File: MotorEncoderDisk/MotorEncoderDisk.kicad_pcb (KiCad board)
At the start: 2 copper layers, 28.2 x 28.2 mm, 1 part

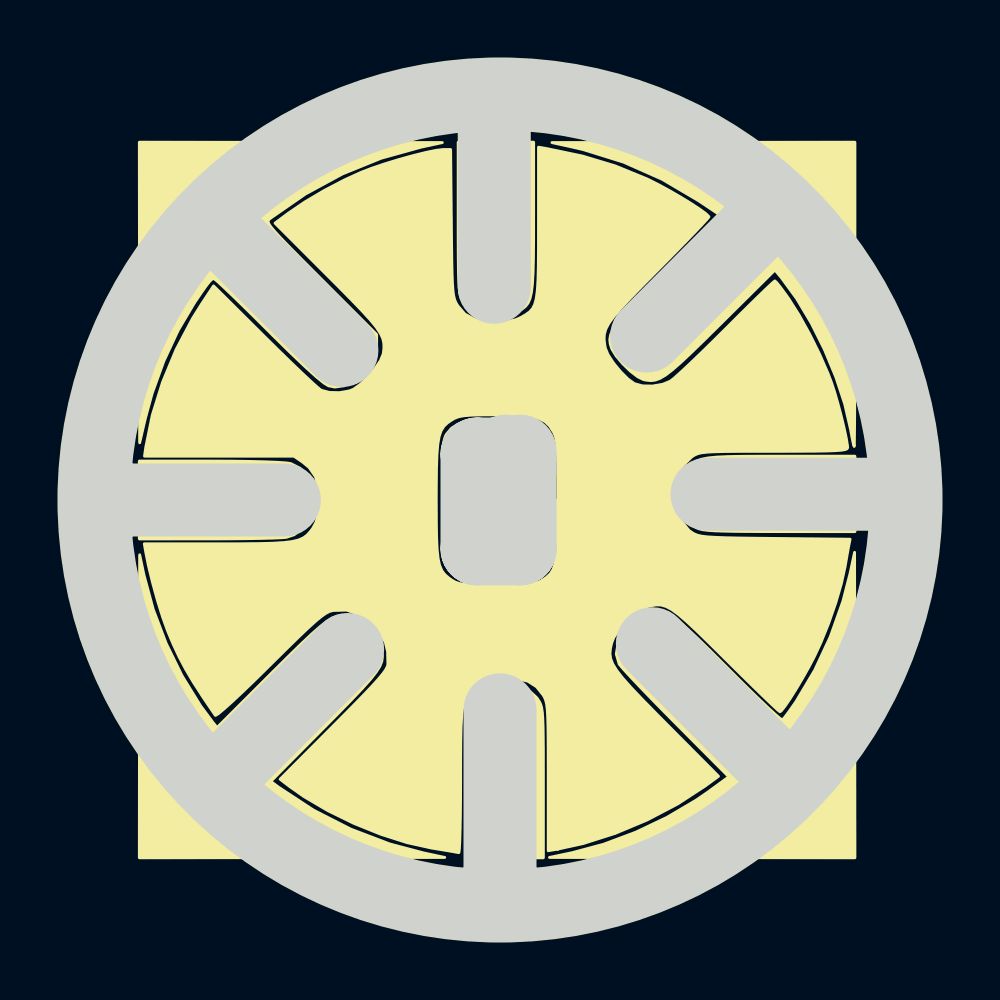
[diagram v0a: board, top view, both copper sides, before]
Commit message: Changed board outline layer to conform to OSHPark rules
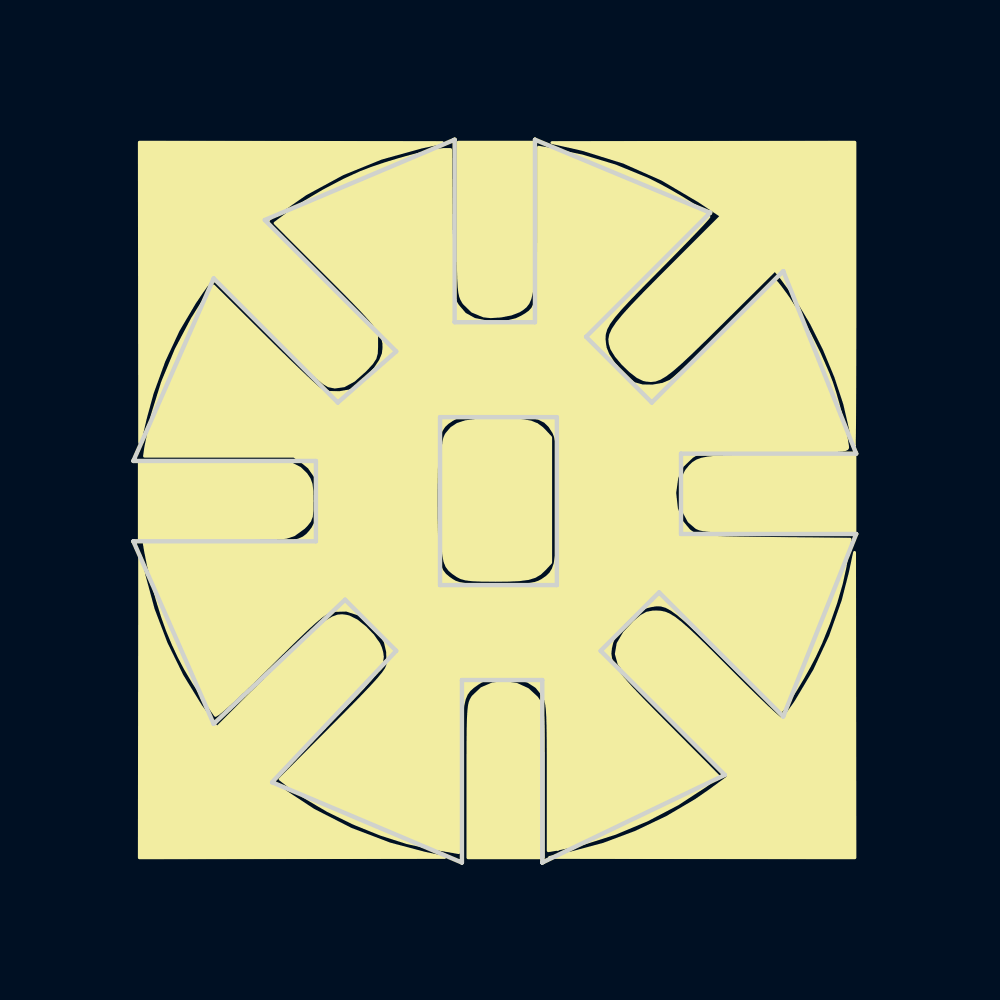
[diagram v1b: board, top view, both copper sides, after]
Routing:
- net (no net): track 0.00 -> 12.9 mm, vias 0 -> 2
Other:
- board size 28.2 x 28.2 mm -> 25.1 x 25.1 mm
- board text added: "C"
- board text added: "CE"
- board text added: "D"
- board text added: "E"
- board text added: "Motor"
- board text added: "N"
- board text added: "O"
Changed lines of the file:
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@@
-(kicad_pcb (version 4) (host pcbnew 0.201506122246+5743~23~ubuntu14.10.1-product)
+(kicad_pcb (version 4) (host pcbnew 0.201505220134+5676~23~ubuntu14.04.1-product)
   (general
     (links 0)
     (no_connects 0)
-    (area 0 0 0 0)
+    (area 113.969799 83.403999 139.396001 108.796001)
     (thickness 1.6)
-    (drawings 14)
-    (tracks 0)
+    (drawings 47)
+    (tracks 11)
     (zones 0)
     (modules 1)
@@
     (35 F.Paste user)
     (36 B.SilkS user)
-    (37 F.SilkS user)
+    (37 F.SilkS user hide)
     (38 B.Mask user)
     (39 F.Mask user)
@@
     (trace_min 0.2)
     (segment_width 0.2)
-    (edge_width 2.54)
+    (edge_width 0.1524)
     (via_size 0.6)
     (via_drill 0.4)
@@
     (visible_elements FFFFFF7F)
     (pcbplotparams
-      (layerselection 0x00030_80000001)
+      (layerselection 0x010c0_80000001)
       (usegerberextensions false)
       (excludeedgelayer true)
@@
       (outputformat 1)
       (mirror false)
-      (drillshape 1)
+      (drillshape 0)
       (scaleselection 1)
-      (outputdirectory ""))
+      (outputdirectory Gerber))
   )
   (net 0 "")
@@
       (xy 1.862666 2.176606) (xy 1.862666 2.176606)) (layer F.SilkS) (width 0.1))
   )
-  (gr_line (start 121.3 90.9) (end 117 86.6) (angle 90) (layer Edge.Cuts) (width 2.54))
-  (gr_circle (center 126.8 96.1) (end 127.6 82) (layer Edge.Cuts) (width 2.54))
-  (gr_line (start 126.8 103.4) (end 126.8 109.4) (angle 90) (layer Edge.Cuts) (width 2.54))
-  (gr_line (start 132.1 101.1) (end 136.7 105.7) (angle 90) (layer Edge.Cuts) (width 2.54))
-  (gr_line (start 121.5 101.3) (end 117 105.8) (angle 90) (layer Edge.Cuts) (width 2.54))
-  (gr_line (start 126.6 88.7) (end 126.6 83) (angle 90) (layer Edge.Cuts) (width 2.54))
-  (gr_line (start 134 95.9) (end 139.8 95.9) (angle 90) (layer Edge.Cuts) (width 2.54))
-  (gr_line (start 119.3 96.1) (end 112.9 96.1) (angle 90) (layer Edge.Cuts) (width 2.54))
-  (gr_line (start 127 94.5) (end 127 94.4) (angle 90) (layer Edge.Cuts) (width 2.54))
-  (gr_line (start 126 94.5) (end 127 94.5) (angle 90) (layer Edge.Cuts) (width 2.54))
-  (gr_line (start 126 97.8) (end 126 94.5) (angle 90) (layer Edge.Cuts) (width 2.54))
-  (gr_line (start 127.5 97.8) (end 126 97.8) (angle 90) (layer Edge.Cuts) (width 2.54))
-  (gr_line (start 127.5 94.4) (end 127.5 97.8) (angle 90) (layer Edge.Cuts) (width 2.54))
-  (gr_line (start 136 86.3) (end 131.9 90.4) (angle 90) (layer Edge.Cuts) (width 2.54))
+  (gr_text CE (at 126.746 100.584) (layer B.Mask)
+    (effects (font (size 1.5 1.5) (thickness 0.3)) (justify mirror))
+  )
+  (gr_text CE (at 126.746 100.584) (layer B.Cu)
+    (effects (font (size 1.5 1.5) (thickness 0.3)) (justify mirror))
+  )
+  (gr_text Motor (at 126.746 91.44) (layer F.Mask)
+    (effects (font (size 1.5 1.5) (thickness 0.3)))
+  )
+  (gr_text E (at 136.144 92.202) (layer F.Cu)
+    (effects (font (size 1.5 1.5) (thickness 0.3)))
+  )
+  (gr_text D (at 136.144 99.568) (layer F.Cu)
+    (effects (font (size 1.5 1.5) (thickness 0.3)))
+  )
+  (gr_text O (at 130.81 105.41) (layer F.Cu)
+    (effects (font (size 1.5 1.5) (thickness 0.3)))
+  )
+  (gr_text C (at 122.682 105.41) (layer F.Cu)
+    (effects (font (size 1.5 1.5) (thickness 0.3)))
+  )
+  (gr_text N (at 117.348 99.822) (layer F.Cu)
+    (effects (font (size 1.5 1.5) (thickness 0.3)))
+  )
+  (gr_text E (at 116.84 92.202) (layer F.Cu)
+    (effects (font (size 1.5 1.5) (thickness 0.3)))
+  )
+  (gr_text Motor (at 126.746 91.44) (layer F.Cu)
+    (effects (font (size 1.5 1.5) (thickness 0.3)))
+  )
+  (gr_line (start 134.112 86.106) (end 128.016 83.566) (angle 90) (layer Edge.Cuts) (width 0.1524))
+  (gr_line (start 129.794 90.424) (end 134.112 86.106) (angle 90) (layer Edge.Cuts) (width 0.1524))
+  (gr_line (start 132.08 92.71) (end 129.794 90.424) (angle 90) (layer Edge.Cuts) (width 0.1524))
+  (gr_line (start 136.652 88.138) (end 132.08 92.71) (angle 90) (layer Edge.Cuts) (width 0.1524))
+  (gr_line (start 139.192 94.488) (end 136.652 88.138) (angle 90) (layer Edge.Cuts) (width 0.1524))
+  (gr_line (start 133.096 94.488) (end 139.192 94.488) (angle 90) (layer Edge.Cuts) (width 0.1524))
+  (gr_line (start 133.096 97.282) (end 133.096 94.488) (angle 90) (layer Edge.Cuts) (width 0.1524))
+  (gr_line (start 139.192 97.282) (end 133.096 97.282) (angle 90) (layer Edge.Cuts) (width 0.1524))
+  (gr_line (start 136.652 103.632) (end 139.192 97.282) (angle 90) (layer Edge.Cuts) (width 0.1524))
+  (gr_line (start 132.334 99.314) (end 136.652 103.632) (angle 90) (layer Edge.Cuts) (width 0.1524))
+  (gr_line (start 132.08 99.568) (end 132.334 99.314) (angle 90) (layer Edge.Cuts) (width 0.1524))
+  (gr_line (start 130.302 101.346) (end 132.08 99.568) (angle 90) (layer Edge.Cuts) (width 0.1524))
+  (gr_line (start 134.62 105.664) (end 130.302 101.346) (angle 90) (layer Edge.Cuts) (width 0.1524))
+  (gr_line (start 128.27 108.712) (end 134.62 105.664) (angle 90) (layer Edge.Cuts) (width 0.1524))
+  (gr_line (start 128.27 102.362) (end 128.27 108.712) (angle 90) (layer Edge.Cuts) (width 0.1524))
+  (gr_line (start 125.476 102.362) (end 128.27 102.362) (angle 90) (layer Edge.Cuts) (width 0.1524))
+  (gr_line (start 125.476 108.712) (end 125.476 102.362) (angle 90) (layer Edge.Cuts) (width 0.1524))
+  (gr_line (start 118.872 105.918) (end 125.476 108.712) (angle 90) (layer Edge.Cuts) (width 0.1524))
+  (gr_line (start 123.19 101.346) (end 118.872 105.918) (angle 90) (layer Edge.Cuts) (width 0.1524))
+  (gr_line (start 121.412 99.568) (end 123.19 101.346) (angle 90) (layer Edge.Cuts) (width 0.1524))
+  (gr_line (start 116.84 103.886) (end 121.412 99.568) (angle 90) (layer Edge.Cuts) (width 0.1524))
+  (gr_line (start 114.046 97.536) (end 116.84 103.886) (angle 90) (layer Edge.Cuts) (width 0.1524))
+  (gr_line (start 120.396 97.536) (end 114.046 97.536) (angle 90) (layer Edge.Cuts) (width 0.1524))
+  (gr_line (start 120.396 94.742) (end 120.396 97.536) (angle 90) (layer Edge.Cuts) (width 0.1524))
+  (gr_line (start 114.046 94.742) (end 120.396 94.742) (angle 90) (layer Edge.Cuts) (width 0.1524))
+  (gr_line (start 116.84 88.392) (end 114.046 94.742) (angle 90) (layer Edge.Cuts) (width 0.1524))
+  (gr_line (start 121.158 92.71) (end 116.84 88.392) (angle 90) (layer Edge.Cuts) (width 0.1524))
+  (gr_line (start 123.19 90.932) (end 121.158 92.71) (angle 90) (layer Edge.Cuts) (width 0.1524))
+  (gr_line (start 118.618 86.36) (end 123.19 90.932) (angle 90) (layer Edge.Cuts) (width 0.1524))
+  (gr_line (start 125.222 83.566) (end 118.618 86.36) (angle 90) (layer Edge.Cuts) (width 0.1524))
+  (gr_line (start 125.222 89.916) (end 125.222 83.566) (angle 90) (layer Edge.Cuts) (width 0.1524))
+  (gr_line (start 128.016 89.916) (end 125.222 89.916) (angle 90) (layer Edge.Cuts) (width 0.1524))
+  (gr_line (start 128.016 83.566) (end 128.016 89.916) (angle 90) (layer Edge.Cuts) (width 0.1524))
+  (gr_line (start 128.778 99.06) (end 128.778 93.218) (angle 90) (layer Edge.Cuts) (width 0.1524))
+  (gr_line (start 124.714 99.06) (end 128.778 99.06) (angle 90) (layer Edge.Cuts) (width 0.1524))
+  (gr_line (start 124.714 93.218) (end 124.714 99.06) (angle 90) (layer Edge.Cuts) (width 0.1524))
+  (gr_line (start 128.778 93.218) (end 124.714 93.218) (angle 90) (layer Edge.Cuts) (width 0.1524))
+  (via (at 123.19 86.868) (size 0.6) (layers F.Cu B.Cu) (net 0))
+  (via (at 130.048 86.868) (size 0.6) (layers F.Cu B.Cu) (net 0))
+  (segment (start 130.048 86.868) (end 130.048 87.63) (width 0.25) (layer B.Cu) (net 0))
+  (segment (start 128.778 88.9) (end 130.048 87.63) (width 0.25) (layer B.Cu) (net 0))
+  (segment (start 128.778 90.17) (end 128.778 88.9) (width 0.25) (layer B.Cu) (net 0))
+  (segment (start 128.016 90.932) (end 128.778 90.17) (width 0.25) (layer B.Cu) (net 0))
+  (segment (start 124.714 90.932) (end 128.016 90.932) (width 0.25) (layer B.Cu) (net 0))
+  (segment (start 124.206 90.424) (end 124.714 90.932) (width 0.25) (layer B.Cu) (net 0))
+  (segment (start 124.206 88.9) (end 124.206 90.424) (width 0.25) (layer B.Cu) (net 0))
+  (segment (start 123.19 87.884) (end 124.206 88.9) (width 0.25) (layer B.Cu) (net 0))
+  (segment (start 123.19 87.884) (end 123.19 86.868) (width 0.25) (layer B.Cu) (net 0))
 )
